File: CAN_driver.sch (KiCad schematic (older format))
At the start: 36 parts, among them J4 DB9_Female, J5 DB9_Female, J6 DB9_Female, J7 DB9_Female, U1 ADM3053, U3 ADM3053

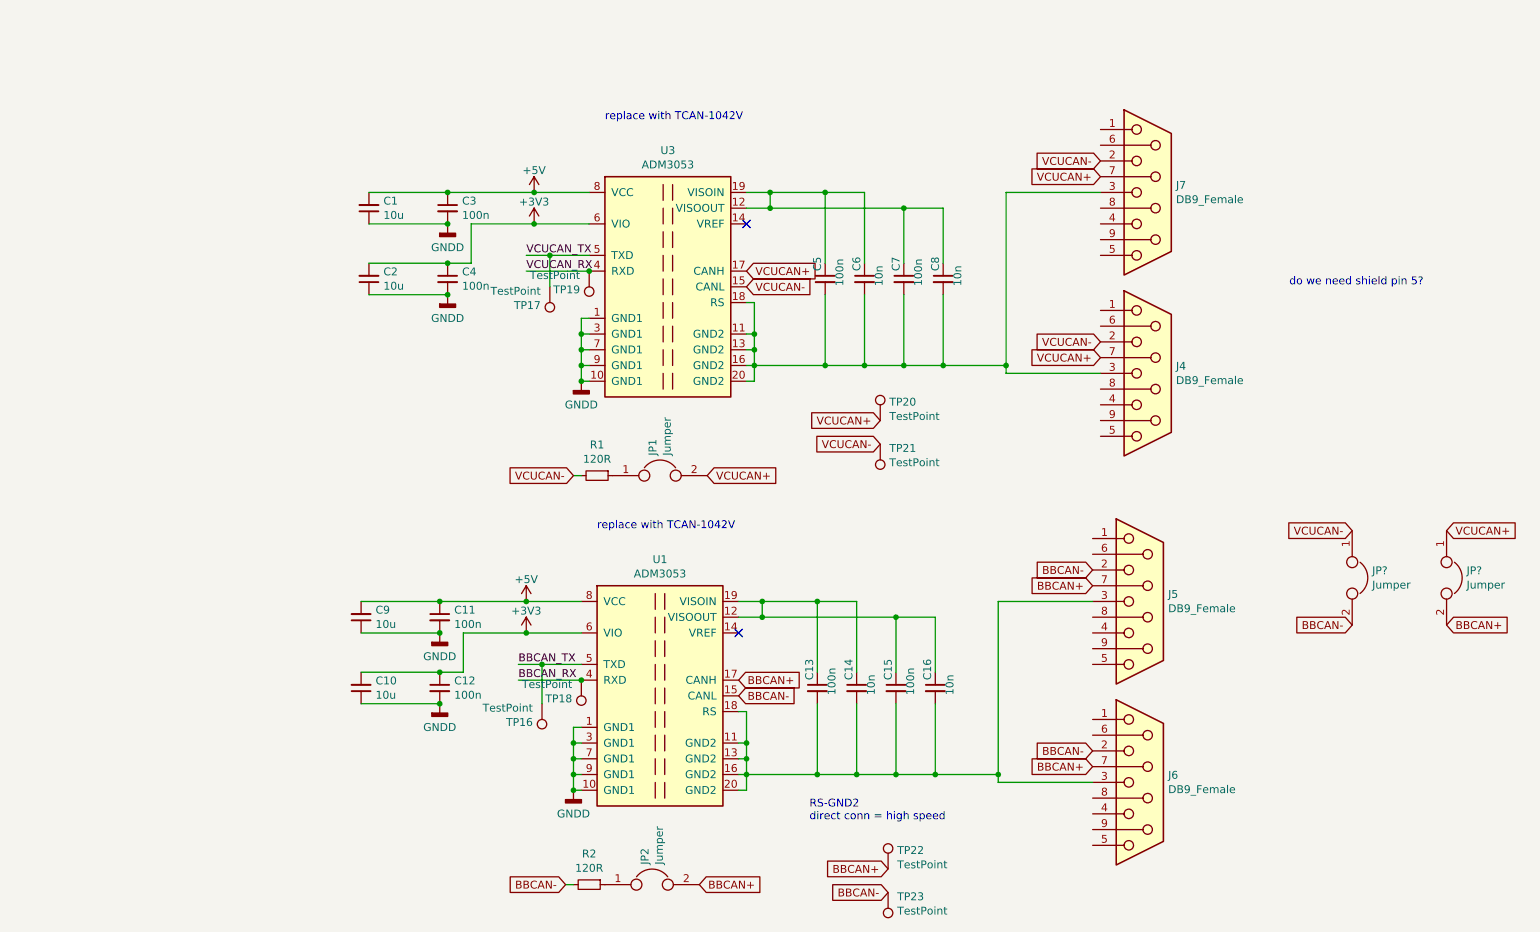
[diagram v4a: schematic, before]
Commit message: changed CAN chips
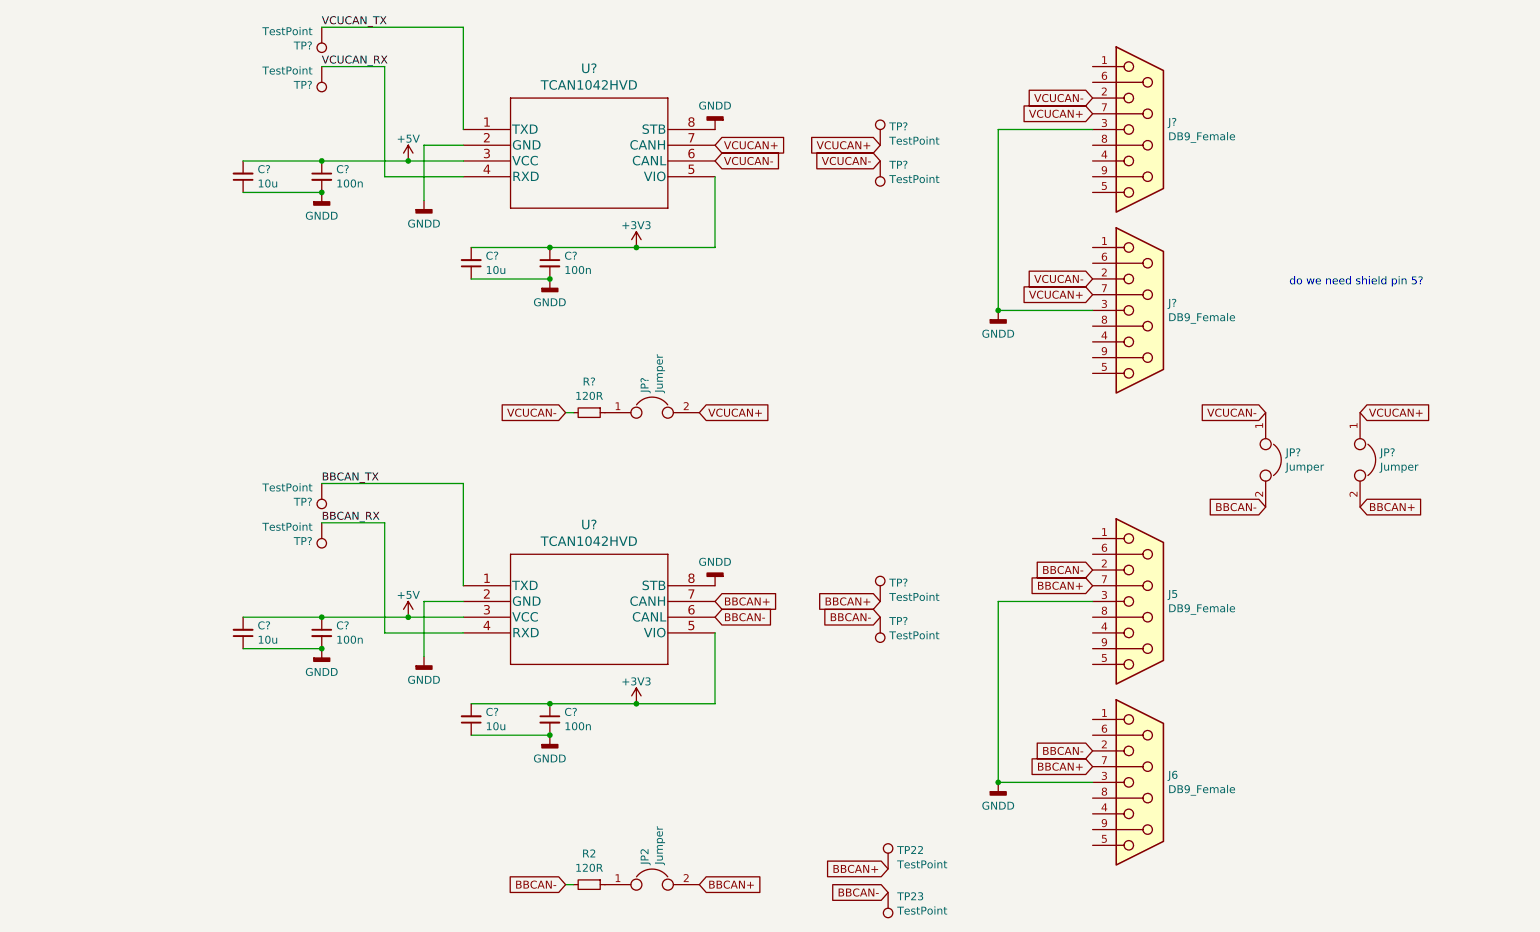
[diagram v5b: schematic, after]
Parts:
- removed C1, C10, C2, C9: 10u, symbol Device:C_Small
- removed C11, C12, C13, C15, C3, C4, C5, C7: 100n, symbol Device:C_Small
- removed C14, C16, C6, C8: 10n, symbol Device:C_Small
- removed J4, J7: DB9_Female, symbol Connector:DB9_Female
- removed JP1: Jumper, symbol Device:Jumper
- removed R1: 120R, symbol Device:R_Small
- removed TP16, TP17, TP18, TP19, TP20, TP21: TestPoint, symbol Connector:TestPoint
- removed U1, U3: ADM3053, Package_SO:SOIC-20W_7.5x12.8mm_P1.27mm, symbol Interface_CAN_LIN:ADM3053
- added C? (x4): 10u, symbol Device:C_Small
- added C? (x4): 100n, symbol Device:C_Small
- added J? (x2): DB9_Female, symbol Connector:DB9_Female
- added JP?: Jumper, symbol Device:Jumper
- added R?: 120R, symbol Device:R_Small
- added TP? (x8): TestPoint, symbol Connector:TestPoint
- added U? (x2): TCAN1042HVD, D0008A_N, symbol TCAN:TCAN1042HVD
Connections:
- net +3V3: now also C?.1, C?.1, C?.2, C?.2, U?.5 (VIO), U?.5 (VIO)
- net +5V: now also C?.1, C?.1, C?.2, C?.2, U?.3 (VCC), U?.3 (VCC)
- net BBCAN+: now also TP?.1, U?.7 (CANH)
- net BBCAN-: now also TP?.1, U?.6 (CANL)
- net BBCAN_RX: now also TP?.1, U?.4 (RXD)
- net BBCAN_TX: now also TP?.1, U?.1 (TXD)
- net GNDD: now also J5.3, J6.3, C?.1, C?.1, C?.1, C?.1, C?.2, C?.2, C?.2, C?.2, J?.3, J?.3, U?.2 (GND), U?.2 (GND), U?.8 (STB), U?.8 (STB)
- net VCUCAN+: now also J?.7, J?.7, JP?.2, TP?.1, U?.7 (CANH)
- net VCUCAN-: now also J?.2, J?.2, R?.2, TP?.1, U?.6 (CANL)
- net VCUCAN_RX: now also TP?.1, U?.4 (RXD)
- net VCUCAN_TX: now also TP?.1, U?.1 (TXD)
- new net: JP?.1, R?.1
- no-connect marks 2 -> 0
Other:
- note removed: "RS-GND2\ndirect conn = high speed"
- note removed: "replace with TCAN-1042V"
- moved on the sheet: JP?

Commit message: removed dac, added jumpers, ready for parting up
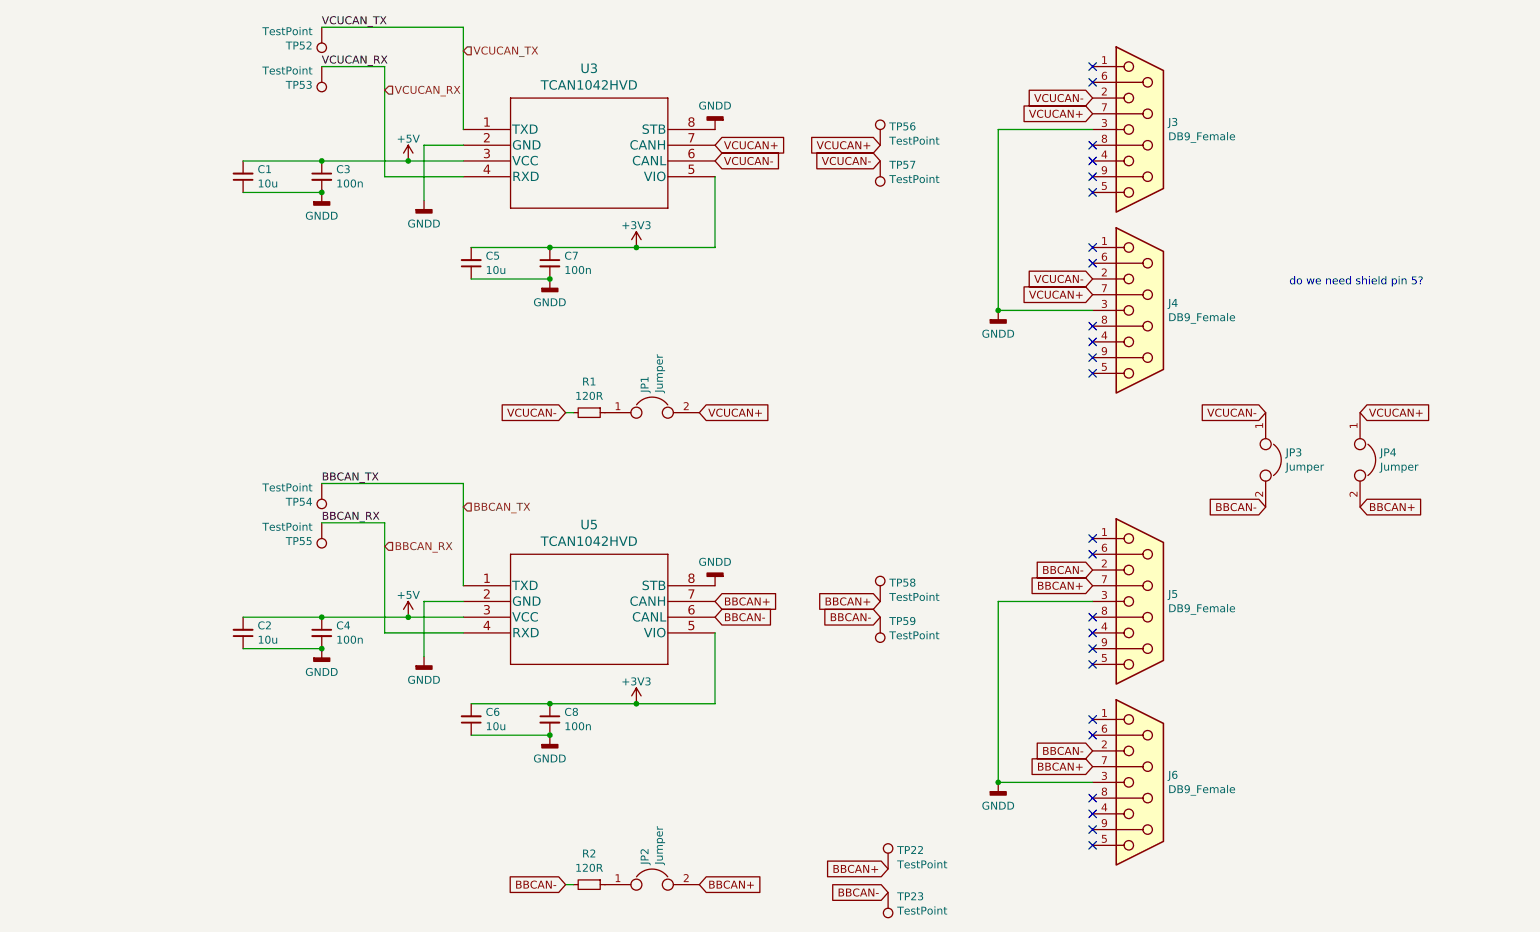
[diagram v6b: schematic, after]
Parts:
- gave numbers to parts that had none: 24
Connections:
- no-connect marks 0 -> 24

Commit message: parts assigned, layout started, CAN and RS232 sides done
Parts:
- removed TP22, TP23: TestPoint, symbol Connector:TestPoint
- C1, C2, C3, C4, C5, C6, C7, C8: footprint (none) -> Capacitor_SMD:C_0805_2012Metric_Pad1.15x1.40mm_HandSolder
- J3, J4, J5, J6: value DB9_Female -> DB9_Male; footprint (none) -> Connector_Dsub:DSUB-9_Male_Horizontal_P2.77x2.84mm_EdgePinOffset7.70mm_Housed_MountingHolesOffset9.12mm; symbol Connector:DB9_Female -> Connector:DB9_Male; Part (none) -> 5747840-3
- JP1, JP2, JP3, JP4: footprint (none) -> Connector_PinHeader_2.00mm:PinHeader_1x03_P2.00mm_Vertical; Part (none) -> SPN02SXCN-RC; PartB (none) -> M22-2510305
- R1, R2: footprint (none) -> Resistor_SMD:R_0805_2012Metric_Pad1.15x1.40mm_HandSolder
- TP52, TP53, TP54, TP55, TP56, TP57, TP58, TP59: footprint (none) -> Connector_PinHeader_2.54mm:PinHeader_1x01_P2.54mm_Vertical
- U3, U5: footprint D0008A_N -> Package_SO:SOIC-8-1EP_3.9x4.9mm_P1.27mm_EP2.41x3.81mm; Part (none) -> 296-48672-1-ND
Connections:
- net BBCAN+: now also J5.8, J6.8; no longer J5.7, J6.7
- net BBCAN-: now also J5.4, J6.4, JP3.1; no longer J5.2, J6.2, JP3.2
- net VCUCAN+: now also J3.8, J4.8; no longer J3.7, J4.7
- net VCUCAN-: now also J3.4, J4.4, JP3.2; no longer J3.2, J4.2, JP3.1
